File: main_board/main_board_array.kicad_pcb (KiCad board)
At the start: 2 copper layers, 81.3 x 91.4 mm, 480 parts, among them U1 STM32G031G8Ux, U2 AMS1117-3.3

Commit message: feat(main_board/led): 高release gerber
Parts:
- removed the C1 at (152.5, 172.4)
- removed the C1 at (111.9, 126.7)
- removed the C1 at (111.9, 142.0)
- removed the C1 at (152.5, 126.7)
- removed the C1 at (152.5, 96.2)
- removed the C1 at (91.6, 126.7)
- removed the C1 at (132.2, 157.2)
- removed the C1 at (132.2, 96.2)
- removed the C1 at (111.9, 157.2)
- removed the C1 at (91.6, 172.4)
- removed the C1 at (91.6, 96.2)
- removed the C1 at (91.6, 142.0)
- removed the C1 at (132.2, 111.5)
- removed the C1 at (91.6, 157.2)
- removed the C1 at (152.5, 142.0)
- removed the C1 at (111.9, 172.4)
- removed the C1 at (91.6, 111.5)
- removed the C1 at (152.5, 157.2)
- removed the C1 at (132.2, 172.4)
- removed the C1 at (111.9, 96.2)
- removed the C1 at (132.2, 142.0)
- removed the C1 at (111.9, 111.5)
- removed the C1 at (152.5, 111.5)
- removed the C1 at (132.2, 126.7)
- removed the C2 at (116.9, 145.2)
- removed the C2 at (96.6, 145.2)
- removed the C2 at (137.2, 130.0)
- removed the C2 at (157.6, 99.5)
- removed the C2 at (157.6, 175.7)
- removed the C2 at (137.2, 175.7)
- removed the C2 at (116.9, 99.5)
- removed the C2 at (116.9, 175.7)
- removed the C2 at (137.2, 160.5)
- removed the C2 at (157.6, 130.0)
- removed the C2 at (116.9, 160.5)
- removed the C2 at (96.6, 130.0)
- removed the C2 at (96.6, 160.5)
- removed the C2 at (116.9, 114.7)
- removed the C2 at (96.6, 99.5)
- removed the C2 at (157.6, 145.2)
- removed the C2 at (157.6, 160.5)
- removed the C2 at (157.6, 114.7)
- removed the C2 at (96.6, 175.7)
- removed the C2 at (137.2, 99.5)
- removed the C2 at (96.6, 114.7)
- removed the C2 at (116.9, 130.0)
- removed the C2 at (137.2, 145.2)
- removed the C2 at (137.2, 114.7)
- removed the C3 at (139.2, 99.5)
- removed the C3 at (159.5, 145.2)
- removed the C3 at (118.9, 99.5)
- removed the C3 at (98.6, 160.5)
- removed the C3 at (118.9, 114.7)
- removed the C3 at (139.2, 160.5)
- removed the C3 at (139.2, 114.7)
- removed the C3 at (98.6, 145.2)
- removed the C3 at (139.2, 175.7)
- removed the C3 at (139.2, 145.2)
- removed the C3 at (118.9, 145.2)
- removed the C3 at (159.5, 130.0)
- removed the C3 at (118.9, 130.0)
- removed the C3 at (98.6, 130.0)
- removed the C3 at (159.5, 175.7)
- removed the C3 at (159.5, 114.7)
- removed the C3 at (98.6, 99.5)
- removed the C3 at (98.6, 175.7)
- removed the C3 at (139.2, 130.0)
- removed the C3 at (98.6, 114.7)
- removed the C3 at (159.5, 160.5)
- removed the C3 at (118.9, 160.5)
- removed the C3 at (118.9, 175.7)
- removed the C3 at (159.5, 99.5)
- removed the C4 at (160.2, 106.1)
- removed the C4 at (119.6, 106.1)
- removed the C4 at (119.6, 90.8)
- removed the C4 at (119.6, 121.3)
- removed the C4 at (139.9, 90.8)
- removed the C4 at (119.6, 136.6)
- removed the C4 at (160.2, 121.3)
- removed the C4 at (99.3, 121.3)
- removed the C4 at (119.6, 167.0)
- removed the C4 at (99.3, 90.8)
- removed the C4 at (160.2, 167.0)
- removed the C4 at (139.9, 151.8)
- removed the C4 at (139.9, 167.0)
- removed the C4 at (139.9, 121.3)
- removed the C4 at (160.2, 90.8)
- removed the C4 at (99.3, 106.1)
- removed the C4 at (160.2, 136.6)
- removed the C4 at (160.2, 151.8)
- removed the C4 at (139.9, 106.1)
- removed the C4 at (99.3, 136.6)
- removed the C4 at (119.6, 151.8)
- removed the C4 at (139.9, 136.6)
- removed the C4 at (99.3, 151.8)
- removed the C4 at (99.3, 167.0)
- removed the C5 at (119.6, 105.2)
- removed the C5 at (160.2, 135.6)
- removed the C5 at (139.9, 89.9)
- removed the C5 at (139.9, 120.4)
- removed the C5 at (99.3, 135.6)
- removed the C5 at (139.9, 166.1)
- removed the C5 at (160.2, 166.1)
- removed the C5 at (99.3, 120.4)
- removed the C5 at (99.3, 105.2)
- removed the C5 at (119.6, 89.9)
- removed the C5 at (160.2, 89.9)
- removed the C5 at (160.2, 150.9)
- removed the C5 at (139.9, 135.6)
- removed the C5 at (119.6, 135.6)
- removed the C5 at (99.3, 89.9)
- removed the C5 at (119.6, 166.1)
- removed the C5 at (139.9, 150.9)
- removed the C5 at (160.2, 105.2)
- removed the C5 at (99.3, 166.1)
- removed the C5 at (139.9, 105.2)
- removed the C5 at (99.3, 150.9)
- removed the C5 at (119.6, 150.9)
- removed the C5 at (160.2, 120.4)
- removed the C5 at (119.6, 120.4)
- removed the H2 at (164.8, 125.0)
- removed the H2 at (144.5, 125.0)
- removed the H2 at (103.8, 140.2)
- removed the H2 at (124.2, 155.4)
- removed the H2 at (103.8, 125.0)
- removed the H2 at (144.5, 140.2)
- removed the H2 at (124.2, 125.0)
- removed the H2 at (124.2, 170.7)
- removed the H2 at (103.8, 170.7)
- removed the H2 at (164.8, 170.7)
- removed the H2 at (103.8, 94.5)
- removed the H2 at (144.5, 109.7)
- removed the H2 at (144.5, 170.7)
- removed the H2 at (124.2, 109.7)
- removed the H2 at (124.2, 140.2)
- removed the H2 at (103.8, 155.4)
- removed the H2 at (164.8, 140.2)
- removed the H2 at (103.8, 109.7)
- removed the H2 at (124.2, 94.5)
- removed the H2 at (164.8, 155.4)
- removed the H2 at (144.5, 155.4)
- removed the H2 at (164.8, 109.7)
- removed the H2 at (144.5, 94.5)
- removed the H2 at (164.8, 94.5)
- removed the JSL1 at (130.4, 87.9)
- removed the JSL1 at (130.4, 133.6)
- removed the JSL1 at (150.7, 118.4)
- removed the JSL1 at (150.7, 87.9)
- removed the JSL1 at (89.7, 133.6)
- removed the JSL1 at (89.7, 118.4)
- removed the JSL1 at (89.7, 103.1)
- removed the JSL1 at (110.0, 148.8)
- removed the JSL1 at (150.7, 164.1)
- removed the JSL1 at (110.0, 87.9)
- removed the JSL1 at (130.4, 164.1)
- removed the JSL1 at (110.0, 118.4)
- removed the JSL1 at (110.0, 164.1)
- removed the JSL1 at (130.4, 118.4)
- removed the JSL1 at (130.4, 103.1)
- removed the JSL1 at (130.4, 148.8)
- removed the JSL1 at (110.0, 103.1)
- removed the JSL1 at (89.7, 164.1)
- removed the JSL1 at (150.7, 148.8)
- removed the JSL1 at (110.0, 133.6)
- removed the JSL1 at (89.7, 148.8)
- removed the JSL1 at (150.7, 133.6)
- removed the JSL1 at (150.7, 103.1)
- removed the JSL1 at (89.7, 87.9)
- removed the R1 at (153.3, 166.6)
- removed the R1 at (112.7, 166.6)
- removed the R1 at (112.7, 151.3)
- removed the R1 at (92.3, 105.6)
- removed the R1 at (112.7, 105.6)
- removed the R1 at (112.7, 136.1)
- removed the R1 at (153.3, 90.3)
- removed the R1 at (112.7, 90.3)
- removed the R1 at (153.3, 105.6)
- removed the R1 at (133.0, 105.6)
- removed the R1 at (112.7, 120.8)
- removed the R1 at (133.0, 90.3)
- removed the R1 at (153.3, 136.1)
- removed the R1 at (153.3, 151.3)
- removed the R1 at (133.0, 166.6)
- removed the R1 at (92.3, 151.3)
- removed the R1 at (133.0, 120.8)
- removed the R1 at (153.3, 120.8)
- removed the R1 at (92.3, 166.6)
- removed the R1 at (133.0, 136.1)
- removed the R1 at (92.3, 136.1)
- removed the R1 at (92.3, 120.8)
- removed the R1 at (92.3, 90.3)
- removed the R1 at (133.0, 151.3)
- removed the R2 at (154.3, 136.1)
- removed the R2 at (113.6, 151.3)
- removed the R2 at (133.9, 120.8)
- removed the R2 at (133.9, 136.1)
- removed the R2 at (133.9, 105.6)
- removed the R2 at (133.9, 151.3)
- removed the R2 at (113.6, 120.8)
- removed the R2 at (93.3, 105.6)
- removed the R2 at (133.9, 166.6)
- removed the R2 at (93.3, 136.1)
- removed the R2 at (93.3, 90.3)
- removed the R2 at (154.3, 151.3)
- removed the R2 at (113.6, 166.6)
- removed the R2 at (93.3, 120.8)
- removed the R2 at (154.3, 120.8)
- removed the R2 at (154.3, 90.3)
- removed the R2 at (113.6, 105.6)
- removed the R2 at (113.6, 136.1)
- removed the R2 at (93.3, 151.3)
- removed the R2 at (154.3, 105.6)
- removed the R2 at (113.6, 90.3)
- removed the R2 at (154.3, 166.6)
- removed the R2 at (93.3, 166.6)
- removed the R2 at (133.9, 90.3)
- removed the R3 at (95.2, 120.8)
- removed the R3 at (156.2, 136.1)
- removed the R3 at (95.2, 105.6)
- removed the R3 at (135.9, 90.3)
- removed the R3 at (115.6, 120.8)
- removed the R3 at (115.6, 90.3)
- removed the R3 at (135.9, 120.8)
- removed the R3 at (156.2, 90.3)
- removed the R3 at (135.9, 151.3)
- removed the R3 at (115.6, 136.1)
- removed the R3 at (156.2, 151.3)
- removed the R3 at (115.6, 151.3)
- removed the R3 at (135.9, 136.1)
- removed the R3 at (156.2, 120.8)
- removed the R3 at (95.2, 166.6)
- removed the R3 at (156.2, 166.6)
- removed the R3 at (156.2, 105.6)
- removed the R3 at (95.2, 151.3)
- removed the R3 at (135.9, 166.6)
- removed the R3 at (95.2, 90.3)
- removed the R3 at (135.9, 105.6)
- removed the R3 at (115.6, 105.6)
- removed the R3 at (95.2, 136.1)
- removed the R3 at (115.6, 166.6)
- removed the R4 at (136.8, 166.6)
- removed the R4 at (116.5, 151.3)
- removed the R4 at (116.5, 105.6)
- removed the R4 at (157.2, 120.8)
- removed the R4 at (157.2, 151.3)
- removed the R4 at (157.2, 136.1)
- removed the R4 at (136.8, 90.3)
- removed the R4 at (136.8, 151.3)
- removed the R4 at (96.2, 136.1)
- removed the R4 at (96.2, 120.8)
- removed the R4 at (116.5, 166.6)
- removed the R4 at (157.2, 105.6)
- removed the R4 at (96.2, 151.3)
- removed the R4 at (96.2, 105.6)
- removed the R4 at (96.2, 166.6)
- removed the R4 at (157.2, 166.6)
- removed the R4 at (136.8, 136.1)
- removed the R4 at (96.2, 90.3)
- removed the R4 at (116.5, 120.8)
- removed the R4 at (136.8, 105.6)
- removed the R4 at (116.5, 136.1)
- removed the R4 at (157.2, 90.3)
- removed the R4 at (116.5, 90.3)
- removed the R4 at (136.8, 120.8)
- removed the R5 at (114.6, 120.8)
- removed the R5 at (94.3, 105.6)
- removed the R5 at (134.9, 166.6)
- removed the R5 at (114.6, 166.6)
- removed the R5 at (155.2, 166.6)
- removed the R5 at (94.3, 120.8)
- removed the R5 at (114.6, 90.3)
- removed the R5 at (155.2, 105.6)
- removed the R5 at (155.2, 136.1)
- removed the R5 at (114.6, 105.6)
- removed the R5 at (134.9, 90.3)
- removed the R5 at (134.9, 136.1)
- removed the R5 at (114.6, 136.1)
- removed the R5 at (155.2, 90.3)
- removed the R5 at (94.3, 90.3)
- removed the R5 at (155.2, 120.8)
- removed the R5 at (94.3, 136.1)
- removed the R5 at (94.3, 151.3)
- removed the R5 at (134.9, 105.6)
- removed the R5 at (155.2, 151.3)
- removed the R5 at (94.3, 166.6)
- removed the R5 at (114.6, 151.3)
- removed the R5 at (134.9, 120.8)
- removed the R5 at (134.9, 151.3)
- removed the R6 at (137.8, 105.6)
- removed the R6 at (158.1, 90.3)
- removed the R6 at (137.8, 136.1)
- removed the R6 at (158.1, 105.6)
- removed the R6 at (137.8, 120.8)
- removed the R6 at (97.2, 90.3)
- removed the R6 at (137.8, 151.3)
- removed the R6 at (158.1, 120.8)
- removed the R6 at (158.1, 166.6)
- removed the R6 at (158.1, 136.1)
- removed the R6 at (117.5, 166.6)
- removed the R6 at (117.5, 90.3)
- removed the R6 at (97.2, 166.6)
- removed the R6 at (158.1, 151.3)
- removed the R6 at (117.5, 151.3)
- removed the R6 at (117.5, 136.1)
- removed the R6 at (97.2, 120.8)
- removed the R6 at (117.5, 120.8)
- removed the R6 at (97.2, 136.1)
- removed the R6 at (117.5, 105.6)
- removed the R6 at (97.2, 151.3)
- removed the R6 at (137.8, 166.6)
- removed the R6 at (137.8, 90.3)
- removed the R6 at (97.2, 105.6)
- removed the REF** at (88.2, 100.2)
- removed the REF** at (130.7, 100.4)
- removed the REF** at (92.0, 100.2)
- removed the REF** at (130.7, 130.9)
- removed the REF** at (153.0, 130.7)
- removed the REF** at (110.4, 176.6)
- removed the REF** at (151.1, 161.3)
- removed the REF** at (110.4, 115.6)
- removed the REF** at (132.7, 100.2)
- removed the REF** at (112.3, 176.4)
- removed the REF** at (110.4, 146.1)
- removed the REF** at (88.2, 130.7)
- removed the REF** at (128.8, 130.7)
- removed the REF** at (151.1, 176.6)
- removed the REF** at (149.1, 130.7)
- removed the REF** at (132.7, 176.4)
- removed the REF** at (110.4, 100.4)
- removed the REF** at (108.5, 115.5)
- removed the REF** at (128.8, 115.5)
- removed the REF** at (90.1, 176.6)
- removed the REF** at (108.5, 176.4)
- removed the REF** at (90.1, 146.1)
- removed the REF** at (88.2, 145.9)
- removed the REF** at (108.5, 100.2)
- removed the REF** at (153.0, 161.2)
- removed the REF** at (108.5, 130.7)
- removed the REF** at (112.3, 145.9)
- removed the REF** at (130.7, 161.3)
- removed the REF** at (92.0, 145.9)
- removed the REF** at (130.7, 115.6)
- removed the REF** at (90.1, 100.4)
- removed the REF** at (151.1, 100.4)
- removed the REF** at (132.7, 145.9)
- removed the REF** at (149.1, 161.2)
- removed the REF** at (110.4, 161.3)
- removed the REF** at (110.4, 130.9)
- removed the REF** at (149.1, 115.5)
- removed the REF** at (90.1, 161.3)
- removed the REF** at (149.1, 145.9)
- removed the REF** at (88.2, 115.5)
- removed the REF** at (153.0, 145.9)
- removed the REF** at (92.0, 130.7)
- removed the REF** at (108.5, 161.2)
- removed the REF** at (132.7, 130.7)
- removed the REF** at (90.1, 115.6)
- removed the REF** at (153.0, 115.5)
- removed the REF** at (90.1, 130.9)
- removed the REF** at (88.2, 176.4)
- removed the REF** at (112.3, 130.7)
- removed the REF** at (128.8, 145.9)
- removed the REF** at (92.0, 115.5)
- removed the REF** at (92.0, 161.2)
- removed the REF** at (112.3, 115.5)
- removed the REF** at (149.1, 176.4)
- removed the REF** at (149.1, 100.2)
- removed the REF** at (112.3, 100.2)
- removed the REF** at (153.0, 100.2)
- removed the REF** at (88.2, 161.2)
- removed the REF** at (132.7, 115.5)
- removed the REF** at (130.7, 176.6)
- removed the REF** at (153.0, 176.4)
- removed the REF** at (128.8, 176.4)
- removed the REF** at (151.1, 130.9)
- removed the REF** at (132.7, 161.2)
- removed the REF** at (130.7, 146.1)
- removed the REF** at (112.3, 161.2)
- removed the REF** at (128.8, 100.2)
- removed the REF** at (151.1, 115.6)
- removed the REF** at (128.8, 161.2)
- removed the REF** at (108.5, 145.9)
- removed the REF** at (92.0, 176.4)
- removed the REF** at (151.1, 146.1)
- removed the S2 at (91.6, 176.0)
- removed the S2 at (132.2, 176.0)
- removed the S2 at (91.6, 115.1)
- removed the S2 at (91.6, 130.3)
- removed the S2 at (132.2, 160.8)
- removed the S2 at (152.6, 115.1)
- removed the S2 at (91.6, 160.8)
- removed the S2 at (152.6, 145.6)
- removed the S2 at (91.6, 145.6)
- removed the S2 at (132.2, 145.6)
- removed the S2 at (91.6, 99.8)
- removed the S2 at (111.9, 130.3)
- removed the S2 at (152.6, 130.3)
- removed the S2 at (152.6, 160.8)
- removed the S2 at (152.6, 176.0)
- removed the S2 at (152.6, 99.8)
- removed the S2 at (111.9, 115.1)
- removed the S2 at (132.2, 115.1)
- removed the S2 at (111.9, 99.8)
- removed the S2 at (132.2, 99.8)
- removed the S2 at (132.2, 130.3)
- removed the S2 at (111.9, 160.8)
- removed the S2 at (111.9, 145.6)
- removed the S2 at (111.9, 176.0)
- removed the S3 at (155.5, 99.8)
- removed the S3 at (94.5, 145.6)
- removed the S3 at (94.5, 115.1)
- removed the S3 at (94.5, 160.8)
- removed the S3 at (155.5, 160.8)
- removed the S3 at (94.5, 130.3)
- removed the S3 at (114.9, 99.8)
- removed the S3 at (135.2, 160.8)
- removed the S3 at (155.5, 115.1)
- removed the S3 at (155.5, 130.3)
- removed the S3 at (135.2, 176.0)
- removed the S3 at (114.9, 176.0)
- removed the S3 at (135.2, 99.8)
- removed the S3 at (155.5, 145.6)
- removed the S3 at (135.2, 130.3)
- removed the S3 at (114.9, 160.8)
- removed the S3 at (114.9, 145.6)
- removed the S3 at (94.5, 176.0)
- removed the S3 at (135.2, 145.6)
- removed the S3 at (155.5, 176.0)
- removed the S3 at (114.9, 130.3)
- removed the S3 at (94.5, 99.8)
- removed the S3 at (135.2, 115.1)
- removed the S3 at (114.9, 115.1)
- removed the U1 at (98.1, 139.9)
- removed the U1 at (118.4, 170.4)
- removed the U1 at (138.7, 155.1)
- removed the U1 at (138.7, 170.4)
- removed the U1 at (98.1, 170.4)
- removed the U1 at (159.1, 139.9)
- removed the U1 at (159.1, 94.2)
- removed the U1 at (118.4, 124.7)
- removed the U1 at (98.1, 94.2)
- removed the U1 at (159.1, 124.7)
- removed the U1 at (138.7, 94.2)
- removed the U1 at (159.1, 155.1)
- removed the U1 at (159.1, 170.4)
- removed the U1 at (98.1, 155.1)
- removed the U1 at (118.4, 109.4)
- removed the U1 at (138.7, 109.4)
- removed the U1 at (118.4, 139.9)
- removed the U1 at (98.1, 109.4)
- removed the U1 at (118.4, 94.2)
- removed the U1 at (118.4, 155.1)
- removed the U1 at (138.7, 124.7)
- removed the U1 at (138.7, 139.9)
- removed the U1 at (159.1, 109.4)
- removed the U1 at (98.1, 124.7)
- removed the U2 at (110.7, 123.3)
- removed the U2 at (110.7, 169.0)
- removed the U2 at (151.4, 92.8)
- removed the U2 at (151.4, 169.0)
- removed the U2 at (90.4, 153.7)
- removed the U2 at (90.4, 123.3)
- removed the U2 at (151.4, 108.0)
- removed the U2 at (90.4, 138.5)
- removed the U2 at (110.7, 138.5)
- removed the U2 at (151.4, 153.7)
- removed the U2 at (151.4, 138.5)
- removed the U2 at (131.1, 108.0)
- removed the U2 at (131.1, 153.7)
- removed the U2 at (131.1, 169.0)
- removed the U2 at (131.1, 92.8)
- removed the U2 at (110.7, 153.7)
- removed the U2 at (131.1, 138.5)
- removed the U2 at (90.4, 108.0)
- removed the U2 at (151.4, 123.3)
- removed the U2 at (131.1, 123.3)
- removed the U2 at (90.4, 92.8)
- removed the U2 at (110.7, 108.0)
- removed the U2 at (110.7, 92.8)
- removed the U2 at (90.4, 169.0)
- added C1: 100n, Capacitor_SMD:C_0402_1005Metric, F.Cu at (120.7, 92.5)
- added C1: 100n, Capacitor_SMD:C_0402_1005Metric, F.Cu at (100.4, 77.2)
- added C1: 100n, Capacitor_SMD:C_0402_1005Metric, F.Cu at (141.1, 77.2)
- added C1: 100n, Capacitor_SMD:C_0402_1005Metric, F.Cu at (120.7, 77.2)
- added C1: 100n, Capacitor_SMD:C_0402_1005Metric, F.Cu at (80.1, 123.0)
- added C1: 100n, Capacitor_SMD:C_0402_1005Metric, F.Cu at (141.1, 123.0)
- added C1: 100n, Capacitor_SMD:C_0402_1005Metric, F.Cu at (80.1, 77.2)
- added C1: 100n, Capacitor_SMD:C_0402_1005Metric, F.Cu at (141.1, 138.2)
- added C1: 100n, Capacitor_SMD:C_0402_1005Metric, F.Cu at (120.7, 107.7)
- added C1: 100n, Capacitor_SMD:C_0402_1005Metric, F.Cu at (80.1, 62.0)
- added C1: 100n, Capacitor_SMD:C_0402_1005Metric, F.Cu at (80.1, 92.5)
- added C1: 100n, Capacitor_SMD:C_0402_1005Metric, F.Cu at (120.7, 62.0)
- added C1: 100n, Capacitor_SMD:C_0402_1005Metric, F.Cu at (100.4, 138.2)
- added C1: 100n, Capacitor_SMD:C_0402_1005Metric, F.Cu at (120.7, 123.0)
- added C1: 100n, Capacitor_SMD:C_0402_1005Metric, F.Cu at (141.1, 62.0)
- added C1: 100n, Capacitor_SMD:C_0402_1005Metric, F.Cu at (100.4, 92.5)
- added C1: 100n, Capacitor_SMD:C_0402_1005Metric, F.Cu at (80.1, 107.7)
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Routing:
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
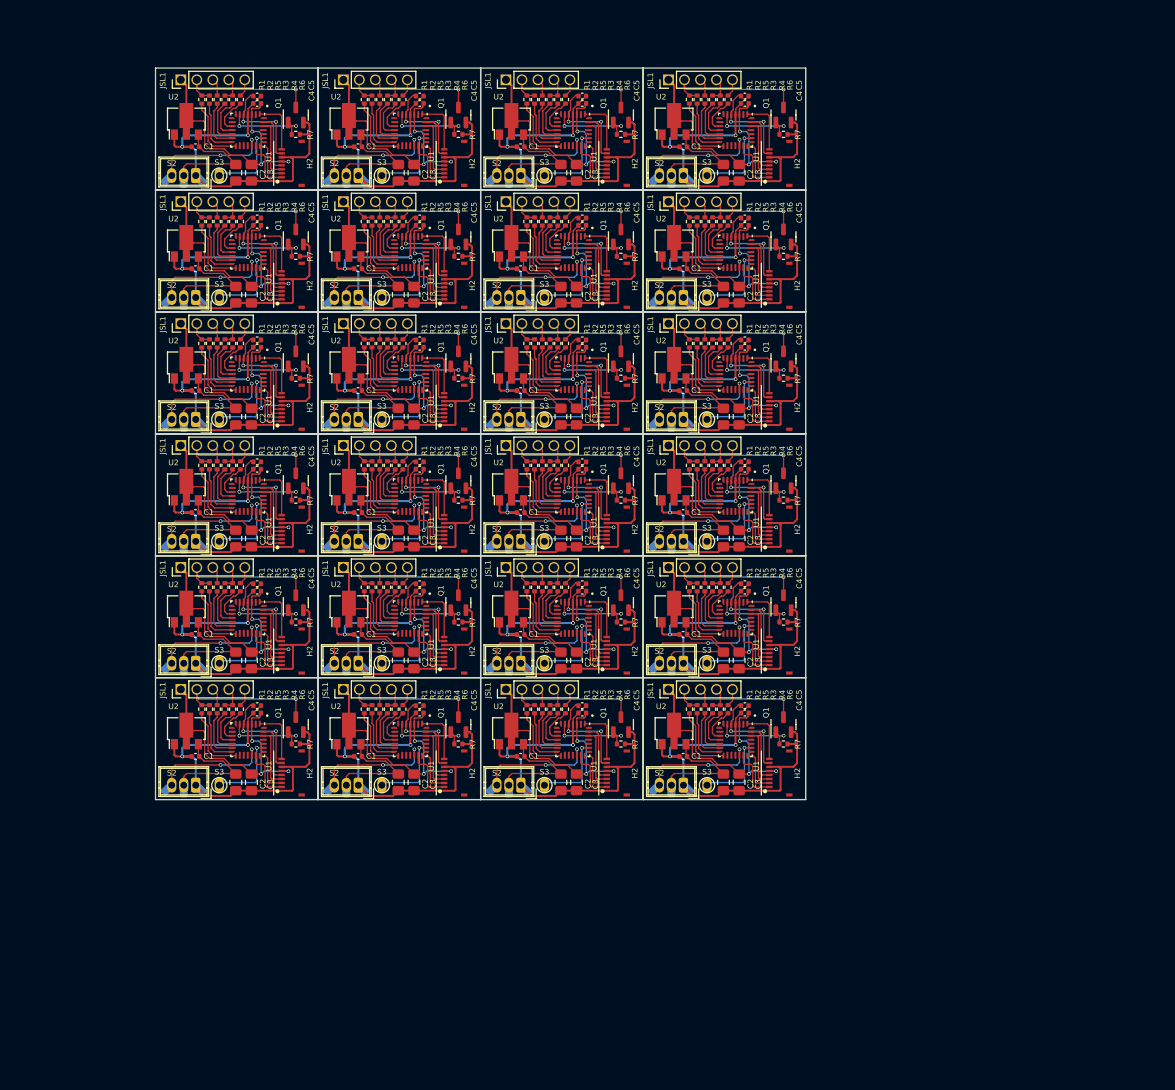
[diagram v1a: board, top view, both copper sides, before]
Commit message: feat: modify logo
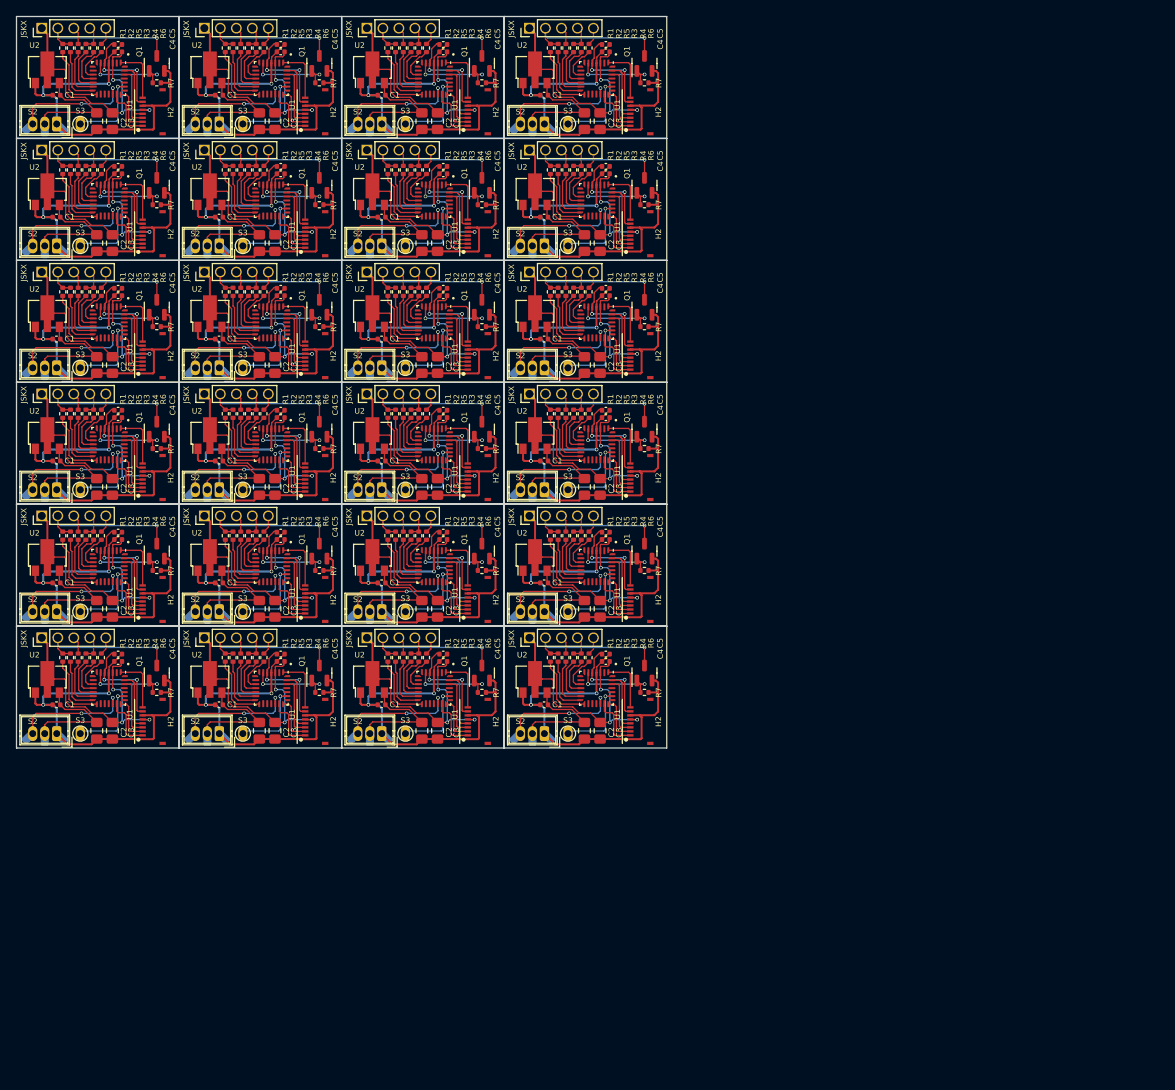
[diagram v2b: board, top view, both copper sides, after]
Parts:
- removed the C1 at (120.7, 92.5)
- removed the C1 at (100.4, 77.2)
- removed the C1 at (141.1, 77.2)
- removed the C1 at (120.7, 77.2)
- removed the C1 at (80.1, 123.0)
- removed the C1 at (141.1, 123.0)
- removed the C1 at (80.1, 77.2)
- removed the C1 at (141.1, 138.2)
- removed the C1 at (120.7, 107.7)
- removed the C1 at (80.1, 62.0)
- removed the C1 at (80.1, 92.5)
- removed the C1 at (120.7, 62.0)
- removed the C1 at (100.4, 138.2)
- removed the C1 at (120.7, 123.0)
- removed the C1 at (141.1, 62.0)
- removed the C1 at (100.4, 92.5)
- removed the C1 at (80.1, 107.7)
- removed the C1 at (80.1, 138.2)
- removed the C1 at (120.7, 138.2)
- removed the C1 at (100.4, 107.7)
- removed the C1 at (100.4, 62.0)
- removed the C1 at (100.4, 123.0)
- removed the C1 at (141.1, 92.5)
- removed the C1 at (141.1, 107.7)
- removed the C2 at (105.5, 126.2)
- removed the C2 at (105.5, 80.5)
- removed the C2 at (146.1, 141.4)
- removed the C2 at (85.1, 65.2)
- removed the C2 at (105.5, 111.0)
- removed the C2 at (125.8, 65.2)
- removed the C2 at (125.8, 111.0)
- removed the C2 at (125.8, 141.4)
- removed the C2 at (146.1, 65.2)
- removed the C2 at (125.8, 80.5)
- removed the C2 at (146.1, 126.2)
- removed the C2 at (105.5, 141.4)
- removed the C2 at (146.1, 80.5)
- removed the C2 at (85.1, 111.0)
- removed the C2 at (85.1, 95.7)
- removed the C2 at (85.1, 141.4)
- removed the C2 at (105.5, 95.7)
- removed the C2 at (146.1, 95.7)
- removed the C2 at (85.1, 126.2)
- removed the C2 at (146.1, 111.0)
- removed the C2 at (125.8, 126.2)
- removed the C2 at (105.5, 65.2)
- removed the C2 at (85.1, 80.5)
- removed the C2 at (125.8, 95.7)
- removed the C3 at (107.4, 95.7)
- removed the C3 at (87.1, 95.7)
- removed the C3 at (127.7, 126.2)
- removed the C3 at (148.1, 111.0)
- removed the C3 at (107.4, 111.0)
- removed the C3 at (87.1, 126.2)
- removed the C3 at (127.7, 111.0)
- removed the C3 at (148.1, 126.2)
- removed the C3 at (148.1, 95.7)
- removed the C3 at (107.4, 65.2)
- removed the C3 at (87.1, 141.4)
- removed the C3 at (107.4, 80.5)
- removed the C3 at (87.1, 65.2)
- removed the C3 at (127.7, 95.7)
- removed the C3 at (127.7, 141.4)
- removed the C3 at (87.1, 80.5)
- removed the C3 at (107.4, 141.4)
- removed the C3 at (148.1, 80.5)
- removed the C3 at (107.4, 126.2)
- removed the C3 at (127.7, 80.5)
- removed the C3 at (87.1, 111.0)
- removed the C3 at (148.1, 65.2)
- removed the C3 at (127.7, 65.2)
- removed the C3 at (148.1, 141.4)
- removed the C4 at (108.1, 71.8)
- removed the C4 at (87.8, 132.8)
- removed the C4 at (87.8, 102.3)
- removed the C4 at (87.8, 117.5)
- removed the C4 at (108.1, 132.8)
- removed the C4 at (128.4, 87.1)
- removed the C4 at (87.8, 71.8)
- removed the C4 at (148.8, 71.8)
- removed the C4 at (108.1, 87.1)
- removed the C4 at (108.1, 117.5)
- removed the C4 at (128.4, 117.5)
- removed the C4 at (148.8, 117.5)
- removed the C4 at (108.1, 56.6)
- removed the C4 at (128.4, 71.8)
- removed the C4 at (148.8, 132.8)
- removed the C4 at (108.1, 102.3)
- removed the C4 at (148.8, 87.1)
- removed the C4 at (128.4, 132.8)
- removed the C4 at (128.4, 56.6)
- removed the C4 at (148.8, 56.6)
- removed the C4 at (87.8, 56.6)
- removed the C4 at (128.4, 102.3)
- removed the C4 at (148.8, 102.3)
- removed the C4 at (87.8, 87.1)
- removed the C5 at (108.1, 70.9)
- removed the C5 at (108.1, 116.6)
- removed the C5 at (87.8, 131.9)
- removed the C5 at (148.8, 131.9)
- removed the C5 at (108.1, 101.4)
- removed the C5 at (148.8, 116.6)
- removed the C5 at (87.8, 116.6)
- removed the C5 at (148.8, 101.4)
- removed the C5 at (128.4, 131.9)
- removed the C5 at (87.8, 55.7)
- removed the C5 at (87.8, 101.4)
- removed the C5 at (128.4, 86.1)
- removed the C5 at (128.4, 101.4)
- removed the C5 at (128.4, 116.6)
- removed the C5 at (148.8, 55.7)
- removed the C5 at (87.8, 86.1)
- removed the C5 at (148.8, 70.9)
- removed the C5 at (128.4, 70.9)
- removed the C5 at (108.1, 55.7)
- removed the C5 at (87.8, 70.9)
- removed the C5 at (148.8, 86.1)
- removed the C5 at (128.4, 55.7)
- removed the C5 at (108.1, 131.9)
- removed the C5 at (108.1, 86.1)
- removed the H2 at (152.8, 109.8)
- removed the H2 at (91.8, 64.1)
- removed the H2 at (112.1, 64.1)
- removed the H2 at (132.4, 140.3)
- removed the H2 at (152.8, 64.1)
- removed the H2 at (112.1, 109.8)
- removed the H2 at (152.8, 140.3)
- removed the H2 at (112.1, 79.3)
- removed the H2 at (91.8, 125.0)
- removed the H2 at (152.8, 94.6)
- removed the H2 at (152.8, 79.3)
- removed the H2 at (91.8, 109.8)
- removed the H2 at (132.4, 109.8)
- removed the H2 at (132.4, 79.3)
- removed the H2 at (132.4, 94.6)
- removed the H2 at (112.1, 140.3)
- removed the H2 at (132.4, 125.0)
- removed the H2 at (91.8, 140.3)
- removed the H2 at (112.1, 125.0)
- removed the H2 at (91.8, 79.3)
- removed the H2 at (152.8, 125.0)
- removed the H2 at (132.4, 64.1)
- removed the H2 at (112.1, 94.6)
- removed the H2 at (91.8, 94.6)
- removed JSL1 (x24): Conn_01x05, Connector_PinHeader_2.00mm:PinHeader_1x05_P2.00mm_Vertical
- removed the Q1 at (113.0, 73.3)
- removed the Q1 at (92.6, 58.0)
- removed the Q1 at (113.0, 58.0)
- removed the Q1 at (153.6, 73.3)
- removed the Q1 at (92.6, 119.0)
- removed the Q1 at (92.6, 73.3)
- removed the Q1 at (133.3, 73.3)
- removed the Q1 at (113.0, 134.2)
- removed the Q1 at (133.3, 134.2)
- removed the Q1 at (92.6, 88.5)
- removed the Q1 at (92.6, 103.8)
- removed the Q1 at (113.0, 103.8)
- removed the Q1 at (133.3, 119.0)
- removed the Q1 at (92.6, 134.2)
- removed the Q1 at (133.3, 58.0)
- removed the Q1 at (133.3, 88.5)
- removed the Q1 at (113.0, 88.5)
- removed the Q1 at (153.6, 103.8)
- removed the Q1 at (153.6, 88.5)
- removed the Q1 at (153.6, 134.2)
- removed the Q1 at (113.0, 119.0)
- removed the Q1 at (153.6, 58.0)
- removed the Q1 at (153.6, 119.0)
- removed the Q1 at (133.3, 103.8)
- removed the R1 at (121.5, 101.8)
- removed the R1 at (101.2, 56.1)
- removed the R1 at (80.9, 71.3)
- removed the R1 at (80.9, 86.6)
- removed the R1 at (141.8, 86.6)
- removed the R1 at (121.5, 132.3)
- removed the R1 at (80.9, 117.1)
- removed the R1 at (101.2, 132.3)
- removed the R1 at (101.2, 117.1)
- removed the R1 at (141.8, 71.3)
- removed the R1 at (101.2, 71.3)
- removed the R1 at (121.5, 56.1)
- removed the R1 at (80.9, 101.8)
- removed the R1 at (141.8, 132.3)
- removed the R1 at (101.2, 101.8)
- removed the R1 at (121.5, 86.6)
- removed the R1 at (141.8, 56.1)
- removed the R1 at (80.9, 56.1)
- removed the R1 at (80.9, 132.3)
- removed the R1 at (141.8, 101.8)
- removed the R1 at (101.2, 86.6)
- removed the R1 at (121.5, 71.3)
- removed the R1 at (141.8, 117.1)
- removed the R1 at (121.5, 117.1)
- removed the R2 at (122.5, 71.3)
- removed the R2 at (142.8, 71.3)
- removed the R2 at (81.8, 86.6)
- removed the R2 at (102.2, 71.3)
- removed the R2 at (122.5, 86.6)
- removed the R2 at (81.8, 132.3)
- removed the R2 at (81.8, 101.8)
- removed the R2 at (122.5, 56.1)
- removed the R2 at (142.8, 86.6)
- removed the R2 at (102.2, 56.1)
- removed the R2 at (142.8, 101.8)
- removed the R2 at (142.8, 117.1)
- removed the R2 at (102.2, 132.3)
- removed the R2 at (81.8, 56.1)
- removed the R2 at (122.5, 101.8)
- removed the R2 at (102.2, 117.1)
- removed the R2 at (102.2, 86.6)
- removed the R2 at (142.8, 56.1)
- removed the R2 at (122.5, 117.1)
- removed the R2 at (142.8, 132.3)
- removed the R2 at (81.8, 117.1)
- removed the R2 at (122.5, 132.3)
- removed the R2 at (102.2, 101.8)
- removed the R2 at (81.8, 71.3)
- removed the R3 at (144.7, 86.6)
- removed the R3 at (124.4, 117.1)
- removed the R3 at (124.4, 101.8)
- removed the R3 at (104.1, 71.3)
- removed the R3 at (83.8, 56.1)
- removed the R3 at (104.1, 101.8)
- removed the R3 at (83.8, 132.3)
- removed the R3 at (104.1, 56.1)
- removed the R3 at (144.7, 101.8)
- removed the R3 at (83.8, 117.1)
- removed the R3 at (144.7, 71.3)
- removed the R3 at (124.4, 86.6)
- removed the R3 at (144.7, 56.1)
- removed the R3 at (104.1, 86.6)
- removed the R3 at (124.4, 132.3)
- removed the R3 at (144.7, 132.3)
- removed the R3 at (104.1, 132.3)
- removed the R3 at (83.8, 71.3)
- removed the R3 at (104.1, 117.1)
- removed the R3 at (124.4, 71.3)
- removed the R3 at (83.8, 101.8)
- removed the R3 at (124.4, 56.1)
- removed the R3 at (83.8, 86.6)
- removed the R3 at (144.7, 117.1)
- removed the R4 at (84.7, 86.6)
- removed the R4 at (84.7, 71.3)
- removed the R4 at (145.7, 71.3)
- removed the R4 at (125.4, 71.3)
- removed the R4 at (105.1, 117.1)
- removed the R4 at (145.7, 56.1)
- removed the R4 at (145.7, 132.3)
- removed the R4 at (105.1, 132.3)
- removed the R4 at (125.4, 86.6)
- removed the R4 at (84.7, 56.1)
- removed the R4 at (84.7, 132.3)
- removed the R4 at (125.4, 117.1)
- removed the R4 at (125.4, 56.1)
- removed the R4 at (145.7, 101.8)
- removed the R4 at (125.4, 101.8)
- removed the R4 at (105.1, 101.8)
- removed the R4 at (145.7, 86.6)
- removed the R4 at (105.1, 71.3)
- removed the R4 at (145.7, 117.1)
- removed the R4 at (105.1, 86.6)
- removed the R4 at (125.4, 132.3)
- removed the R4 at (84.7, 101.8)
- removed the R4 at (84.7, 117.1)
- removed the R4 at (105.1, 56.1)
- removed the R5 at (123.5, 71.3)
- removed the R5 at (82.8, 132.3)
- removed the R5 at (123.5, 56.1)
- removed the R5 at (143.8, 56.1)
- removed the R5 at (82.8, 101.8)
- removed the R5 at (103.1, 132.3)
- removed the R5 at (103.1, 117.1)
- removed the R5 at (82.8, 117.1)
- removed the R5 at (82.8, 56.1)
- removed the R5 at (143.8, 101.8)
- removed the R5 at (123.5, 101.8)
- removed the R5 at (143.8, 117.1)
- removed the R5 at (82.8, 86.6)
- removed the R5 at (103.1, 56.1)
- removed the R5 at (103.1, 101.8)
- removed the R5 at (123.5, 132.3)
- removed the R5 at (143.8, 86.6)
- removed the R5 at (143.8, 132.3)
- removed the R5 at (103.1, 71.3)
- removed the R5 at (103.1, 86.6)
- removed the R5 at (123.5, 117.1)
- removed the R5 at (82.8, 71.3)
- removed the R5 at (143.8, 71.3)
- removed the R5 at (123.5, 86.6)
- removed the R6 at (106.0, 101.8)
- removed the R6 at (146.7, 86.6)
- removed the R6 at (146.7, 132.3)
- removed the R6 at (106.0, 71.3)
- removed the R6 at (85.7, 86.6)
- removed the R6 at (85.7, 71.3)
- removed the R6 at (126.4, 56.1)
- removed the R6 at (146.7, 101.8)
- removed the R6 at (106.0, 117.1)
- removed the R6 at (126.4, 101.8)
- removed the R6 at (146.7, 71.3)
- removed the R6 at (106.0, 86.6)
- removed the R6 at (126.4, 117.1)
- removed the R6 at (85.7, 117.1)
- removed the R6 at (126.4, 71.3)
- removed the R6 at (146.7, 56.1)
- removed the R6 at (146.7, 117.1)
- removed the R6 at (126.4, 132.3)
- removed the R6 at (85.7, 132.3)
- removed the R6 at (85.7, 101.8)
- removed the R6 at (106.0, 56.1)
- removed the R6 at (106.0, 132.3)
- removed the R6 at (85.7, 56.1)
- removed the R6 at (126.4, 86.6)
- removed the R7 at (113.0, 90.9)
- removed the R7 at (92.6, 60.5)
- removed the R7 at (153.6, 136.7)
- removed the R7 at (133.3, 121.4)
- removed the R7 at (133.3, 90.9)
- removed the R7 at (92.6, 90.9)
- removed the R7 at (113.0, 121.4)
- removed the R7 at (92.6, 106.2)
- removed the R7 at (113.0, 136.7)
- removed the R7 at (153.6, 90.9)
- removed the R7 at (133.3, 60.5)
- removed the R7 at (153.6, 75.7)
- removed the R7 at (113.0, 106.2)
- removed the R7 at (133.3, 136.7)
- removed the R7 at (113.0, 60.5)
- removed the R7 at (92.6, 75.7)
- removed the R7 at (133.3, 75.7)
- removed the R7 at (153.6, 106.2)
- removed the R7 at (92.6, 136.7)
- removed the R7 at (153.6, 121.4)
- removed the R7 at (92.6, 121.4)
- removed the R7 at (153.6, 60.5)
- removed the R7 at (133.3, 106.2)
- removed the R7 at (113.0, 75.7)
- removed the REF** at (100.9, 81.2)
- removed the REF** at (76.7, 81.2)
- removed the REF** at (137.7, 142.2)
- removed the REF** at (76.7, 126.9)
- removed the REF** at (117.3, 66.0)
- removed the REF** at (76.7, 111.7)
- removed the REF** at (100.9, 111.7)
- removed the REF** at (139.6, 66.1)
- removed the REF** at (117.3, 81.2)
- removed the REF** at (137.7, 126.9)
- removed the REF** at (100.9, 142.2)
- removed the REF** at (97.0, 142.2)
- removed the REF** at (97.0, 81.2)
- removed the REF** at (80.5, 66.0)
- removed the REF** at (99.0, 96.6)
- removed the REF** at (141.5, 126.9)
- removed the REF** at (141.5, 66.0)
- removed the REF** at (100.9, 66.0)
- removed the REF** at (99.0, 142.3)
- removed the REF** at (139.6, 127.1)
- removed the REF** at (117.3, 96.5)
- removed the REF** at (117.3, 126.9)
- removed the REF** at (139.6, 111.9)
- removed the REF** at (97.0, 66.0)
- removed the REF** at (99.0, 81.4)
- removed the REF** at (119.3, 96.6)
- removed the REF** at (80.5, 96.5)
- removed the REF** at (80.5, 81.2)
- removed the REF** at (137.7, 66.0)
- removed the REF** at (78.6, 111.9)
- removed the REF** at (119.3, 66.1)
- removed the REF** at (119.3, 127.1)
- removed the REF** at (119.3, 81.4)
- removed the REF** at (141.5, 111.7)
- removed the REF** at (121.2, 66.0)
- removed the REF** at (119.3, 111.9)
- removed the REF** at (121.2, 126.9)
- removed the REF** at (78.6, 81.4)
- removed the REF** at (141.5, 81.2)
- removed the REF** at (80.5, 142.2)
- removed the REF** at (97.0, 111.7)
- removed the REF** at (76.7, 142.2)
- removed the REF** at (78.6, 66.1)
- removed the REF** at (78.6, 142.3)
- removed the REF** at (121.2, 81.2)
- removed the REF** at (139.6, 142.3)
- removed the REF** at (117.3, 111.7)
- removed the REF** at (80.5, 126.9)
- removed the REF** at (141.5, 96.5)
- removed the REF** at (121.2, 142.2)
- removed the REF** at (121.2, 96.5)
- removed the REF** at (137.7, 111.7)
- removed the REF** at (100.9, 96.5)
- removed the REF** at (119.3, 142.3)
- removed the REF** at (80.5, 111.7)
- removed the REF** at (99.0, 127.1)
- removed the REF** at (121.2, 111.7)
- removed the REF** at (139.6, 81.4)
- removed the REF** at (99.0, 111.9)
- removed the REF** at (100.9, 126.9)
- removed the REF** at (99.0, 66.1)
- removed the REF** at (137.7, 81.2)
- removed the REF** at (76.7, 96.5)
- removed the REF** at (141.5, 142.2)
- removed the REF** at (78.6, 96.6)
- removed the REF** at (117.3, 142.2)
- removed the REF** at (78.6, 127.1)
- removed the REF** at (97.0, 126.9)
- removed the REF** at (97.0, 96.5)
- removed the REF** at (76.7, 66.0)
- removed the REF** at (139.6, 96.6)
- removed the REF** at (137.7, 96.5)
- removed the S2 at (141.1, 96.1)
- removed the S2 at (141.1, 141.8)
- removed the S2 at (80.1, 126.6)
- removed the S2 at (120.8, 111.3)
- removed the S2 at (80.1, 80.8)
- removed the S2 at (141.1, 126.6)
- removed the S2 at (100.5, 96.1)
- removed the S2 at (100.5, 126.6)
- removed the S2 at (80.1, 96.1)
- removed the S2 at (80.1, 65.6)
- removed the S2 at (120.8, 126.6)
- removed the S2 at (80.1, 111.3)
- removed the S2 at (141.1, 65.6)
- removed the S2 at (80.1, 141.8)
- removed the S2 at (100.5, 80.8)
- removed the S2 at (100.5, 141.8)
- removed the S2 at (100.5, 111.3)
- removed the S2 at (141.1, 111.3)
- removed the S2 at (100.5, 65.6)
- removed the S2 at (120.8, 80.8)
- removed the S2 at (120.8, 96.1)
- removed the S2 at (120.8, 65.6)
- removed the S2 at (141.1, 80.8)
- removed the S2 at (120.8, 141.8)
- removed the S3 at (123.7, 111.3)
- removed the S3 at (123.7, 96.1)
- removed the S3 at (83.1, 96.1)
- removed the S3 at (123.7, 141.8)
- removed the S3 at (144.0, 65.6)
- removed the S3 at (123.7, 65.6)
- removed the S3 at (123.7, 126.6)
- removed the S3 at (144.0, 126.6)
- removed the S3 at (144.0, 141.8)
- removed the S3 at (103.4, 96.1)
- removed the S3 at (83.1, 80.8)
- removed the S3 at (144.0, 96.1)
- removed the S3 at (83.1, 141.8)
- removed the S3 at (83.1, 111.3)
- removed the S3 at (123.7, 80.8)
- removed the S3 at (83.1, 65.6)
- removed the S3 at (144.0, 80.8)
- removed the S3 at (144.0, 111.3)
- removed the S3 at (103.4, 141.8)
- removed the S3 at (103.4, 111.3)
- removed the S3 at (103.4, 126.6)
- removed the S3 at (103.4, 80.8)
- removed the S3 at (103.4, 65.6)
- removed the S3 at (83.1, 126.6)
- removed the U1 at (107.0, 75.2)
- removed the U1 at (127.3, 90.4)
- removed the U1 at (127.3, 120.9)
- removed the U1 at (107.0, 105.6)
- removed the U1 at (147.6, 120.9)
- removed the U1 at (86.6, 59.9)
- removed the U1 at (107.0, 90.4)
- removed the U1 at (147.6, 90.4)
- removed the U1 at (127.3, 75.2)
- removed the U1 at (86.6, 90.4)
- removed the U1 at (86.6, 136.1)
- removed the U1 at (107.0, 59.9)
- removed the U1 at (107.0, 136.1)
- removed the U1 at (86.6, 105.6)
- removed the U1 at (147.6, 105.6)
- removed the U1 at (147.6, 59.9)
- removed the U1 at (127.3, 105.6)
- removed the U1 at (86.6, 75.2)
- removed the U1 at (107.0, 120.9)
- removed the U1 at (147.6, 136.1)
- removed the U1 at (86.6, 120.9)
- removed the U1 at (147.6, 75.2)
- removed the U1 at (127.3, 136.1)
- removed the U1 at (127.3, 59.9)
- removed the U2 at (79.0, 104.3)
- removed the U2 at (119.6, 58.5)
- removed the U2 at (99.3, 134.7)
- removed the U2 at (99.3, 58.5)
- removed the U2 at (79.0, 119.5)
- removed the U2 at (139.9, 119.5)
- removed the U2 at (139.9, 134.7)
- removed the U2 at (99.3, 89.0)
- removed the U2 at (79.0, 73.8)
- removed the U2 at (139.9, 89.0)
- removed the U2 at (99.3, 104.3)
- removed the U2 at (119.6, 104.3)
- removed the U2 at (79.0, 89.0)
- removed the U2 at (119.6, 134.7)
- removed the U2 at (99.3, 119.5)
- removed the U2 at (119.6, 73.8)
- removed the U2 at (79.0, 134.7)
- removed the U2 at (119.6, 89.0)
- removed the U2 at (99.3, 73.8)
- removed the U2 at (139.9, 73.8)
- removed the U2 at (139.9, 104.3)
- removed the U2 at (79.0, 58.5)
- removed the U2 at (119.6, 119.5)
- removed the U2 at (139.9, 58.5)
- added C1: 100n, Capacitor_SMD:C_0402_1005Metric, F.Cu at (123.7, 131.8)
- added C1: 100n, Capacitor_SMD:C_0402_1005Metric, F.Cu at (62.7, 86.0)
- added C1: 100n, Capacitor_SMD:C_0402_1005Metric, F.Cu at (123.7, 55.6)
- added C1: 100n, Capacitor_SMD:C_0402_1005Metric, F.Cu at (62.7, 101.3)
- added C1: 100n, Capacitor_SMD:C_0402_1005Metric, F.Cu at (103.4, 116.5)
- added C1: 100n, Capacitor_SMD:C_0402_1005Metric, F.Cu at (83.0, 131.8)
- added C1: 100n, Capacitor_SMD:C_0402_1005Metric, F.Cu at (83.0, 70.8)
- added C1: 100n, Capacitor_SMD:C_0402_1005Metric, F.Cu at (123.7, 116.5)
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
